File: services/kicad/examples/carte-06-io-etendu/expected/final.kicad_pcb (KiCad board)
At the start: 2 copper layers, 80 x 60 mm, 35 parts, among them J1 IN_5V, J10 IO0, J11 IO1, J2 SWD, U1 STM32F103C8T6, U2 AMS1117-3.3

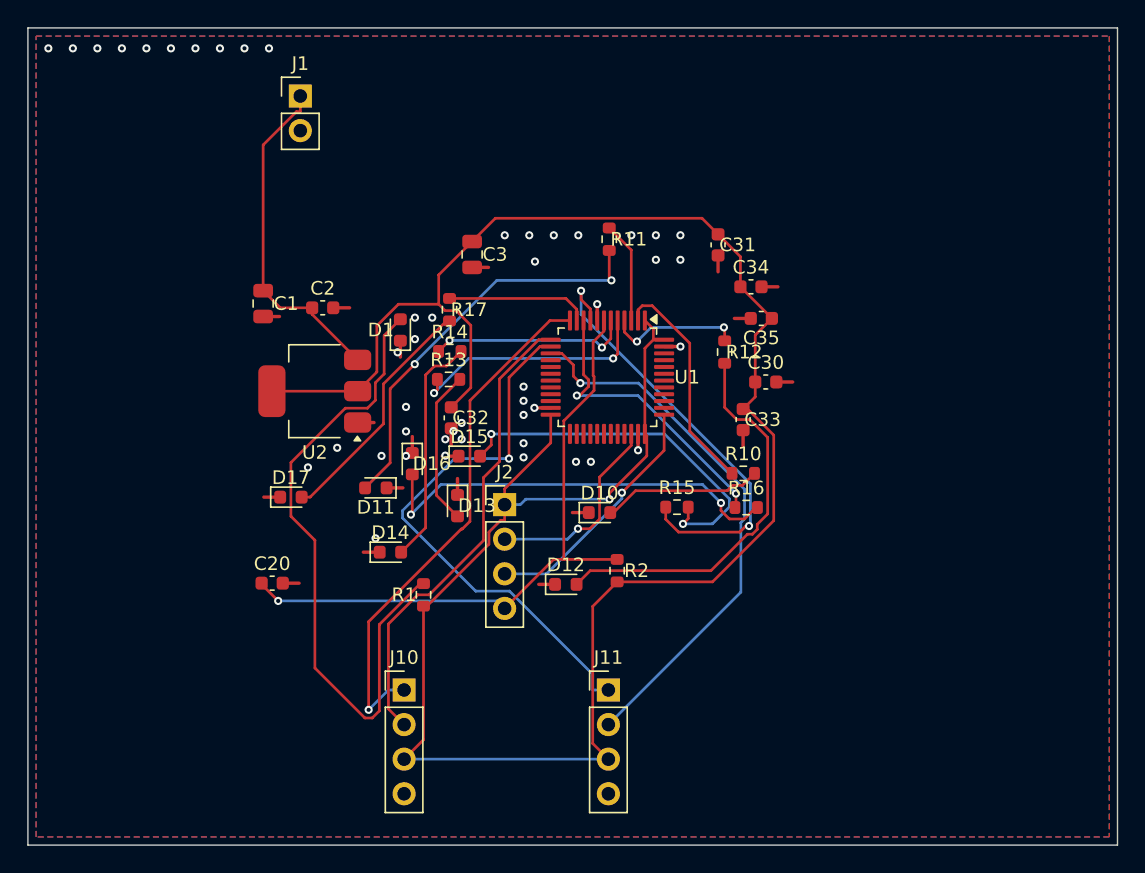
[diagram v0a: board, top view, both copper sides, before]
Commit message: fix(routing): GND route par defaut, plan sur reglage -- sites et tests alignes
Quatre sites de routing.py lisaient encore `_nets_confies_au_plan()` au
lieu de la constante `_NETS_CONFIES_AU_PLAN` que le module reaffecte et que
les tests remplacent : le reglage n atteignait pas ces sites. L escalade
n avait plus de repli vers `_NETS_DE_PLAN_CONNUS` (une connexion GND
manquante doit pouvoir escalader quand GND est route).

Tests encodant l ancienne strategie (GND confie au plan) recrits : les deux
cas sont couverts, GND route par defaut (decision utilisateur du 2026-09-10,
reference STM32 Astra + docs/methodologie-routage.md) et GND confie au plan
sur le reglage `gnd_confie_au_plan`.

`_reattribuer_les_decouplages` rend intact ce qui n est pas une liste.
Deux tests de journal Freerouting comparaient un chemin Windows a un
entrypoint POSIX : `as_posix()`.

Cartes 01, 02, 03, 04, 06 regenerees avec GND route : 100 % routees,
0 erreur DRC, fabricables ; placement.kicad_pcb livre pour chacune.

1630 passed, 2 skipped.

Co-Authored-By: Claude Fable 5.1 <noreply@anthropic.com>
Claude-Session: https://claude.ai/code/session_01TnMqm4La2CxQHHB5K8aSSV
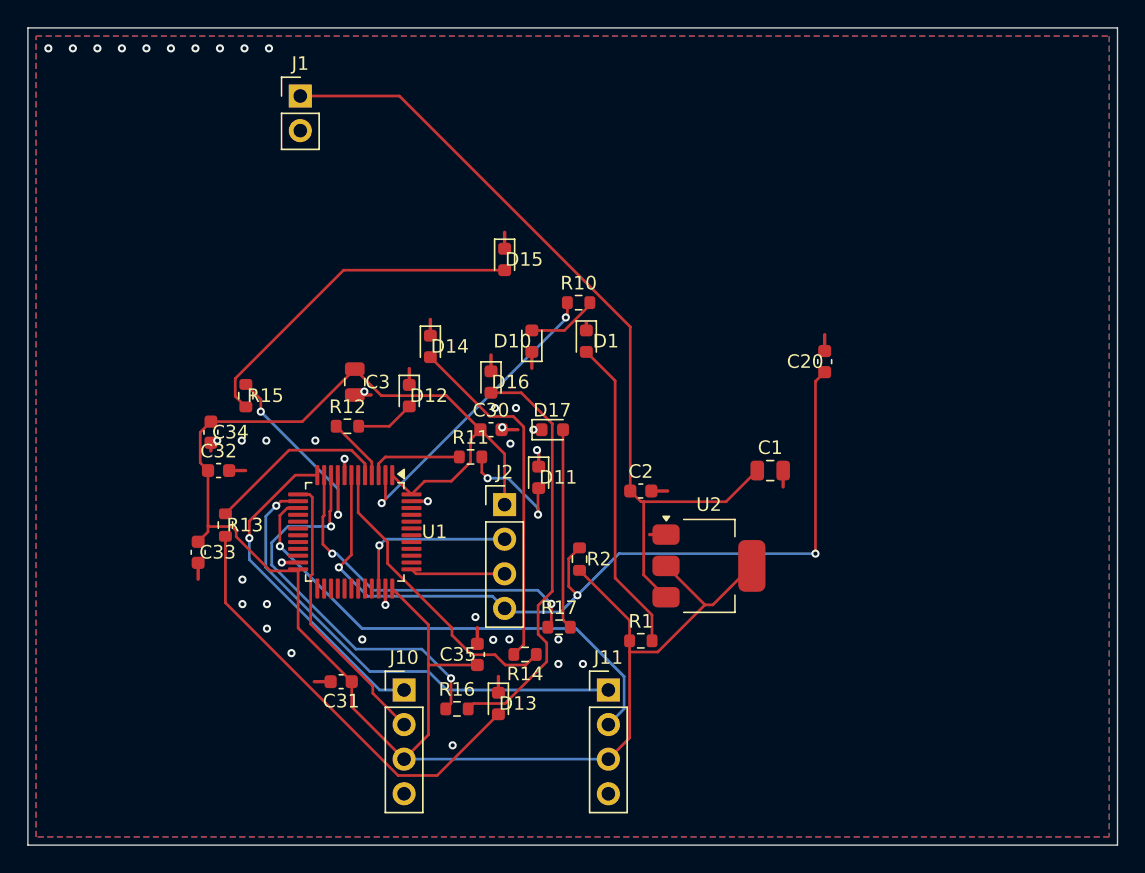
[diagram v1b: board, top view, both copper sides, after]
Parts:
- moved C20 43.7 mm to (167.0, 99.5), turned to 90 degrees
- moved C31 42.4 mm to (131.5, 123.0), turned to 180 degrees
- moved C33 41.2 mm to (121.0, 113.5)
- moved C34 41.1 mm to (121.9, 104.7), turned to -90 degrees
- moved C1 39.2 mm to (163.0, 107.5), turned to 0 degrees
- moved R15 32.7 mm to (124.5, 102.0), turned to -90 degrees
- moved C35 32.3 mm to (141.5, 121.0), turned to 90 degrees
- moved U2 31.7 mm to (158.5, 114.5), turned to 0 degrees
- moved R12 28.2 mm to (132.0, 104.2), turned to 0 degrees
- moved C2 27.0 mm to (153.5, 109.0)
- moved R16 25.9 mm to (140.0, 125.0)
- moved R17 24.7 mm to (147.5, 119.0), turned to 0 degrees
- moved R14 22.9 mm to (145.0, 121.0), turned to 180 degrees
- moved U1 21.7 mm to (132.5, 112.0)
- moved C30 20.5 mm to (142.5, 104.5)
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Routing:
- net VIN: track 24.9 -> 61.6 mm
- net +3V3: track 172.1 -> 139.1 mm, vias 1 -> 0
- net LEDA2: track 29.3 -> 4.32 mm
- net LED_PWR: track 47.9 -> 23.2 mm
- net LEDA1: track 29.9 -> 8.79 mm
- net LEDA3: track 11.4 -> 32.0 mm
- net IO_L5: track 32.5 -> 15.3 mm
- net NRST: track 47.2 -> 63.0 mm, vias 1 -> 3
- net IO_L7: track 10.5 -> 25.5 mm, vias 0 -> 2
- net EXT0_1: track 38.8 -> 24.5 mm
- net EXT0_2: track 34.7 -> 20.7 mm
- net SWCLK: track 18.3 -> 6.97 mm, vias 1 -> 0
- net LEDA4: track 17.1 -> 26.0 mm
- net IO_L6: track 21.9 -> 29.3 mm
- net IO_L4: track 14.8 -> 22.0 mm, vias 2 -> 0
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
